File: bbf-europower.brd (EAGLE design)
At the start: 16.5 x 52.1 mm, 9 parts

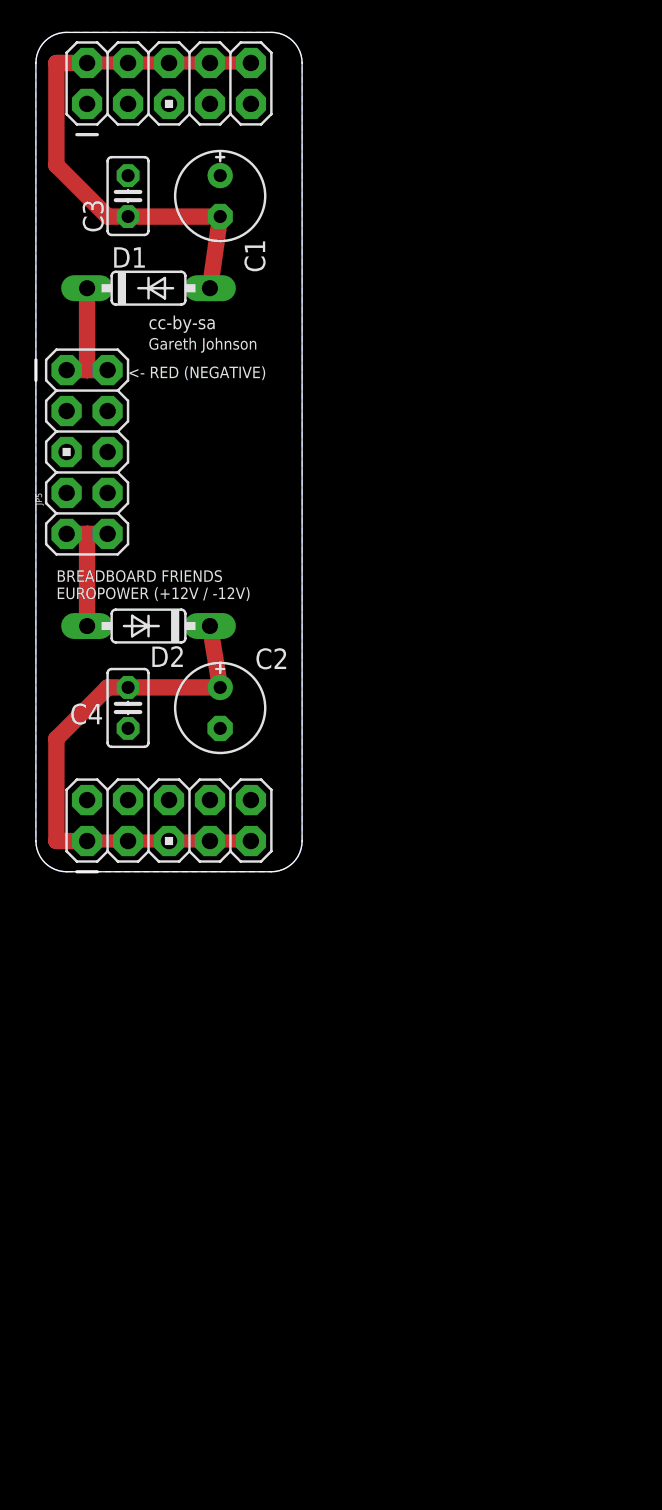
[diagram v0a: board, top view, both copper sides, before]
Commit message: Add files via upload
Through-hole versions of Thomas Hopman's revision of the bbf-europower.
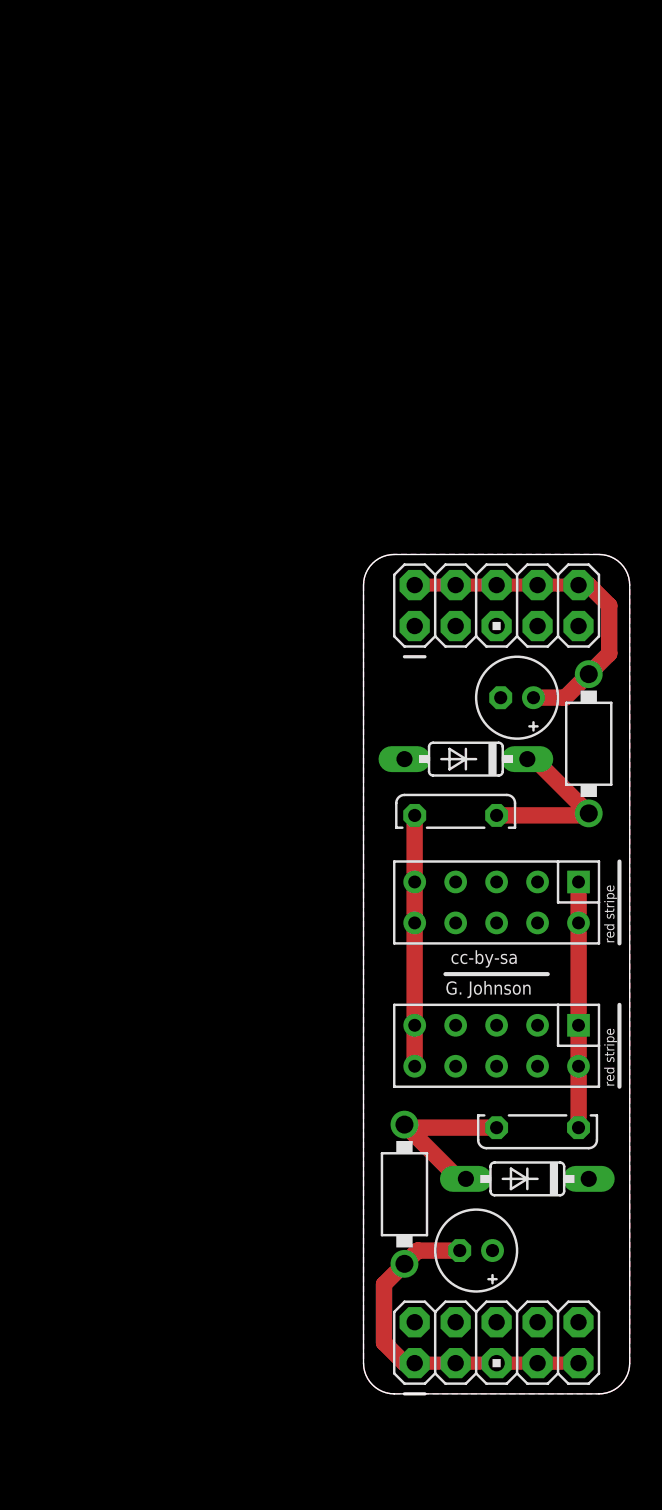
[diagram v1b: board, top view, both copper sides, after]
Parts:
- removed C3, C4: (no value), TomW:C025-025X050
- removed JP5: M05X2PTH, SparkFun:AVR_ICSP
- added +FUSE1: +FUSE, TomW:C050H075X075
- added -FUSE1: -FUSE, TomW:C050H075X075
- added J1, J2: CON_HEADER_2X05-PTH, tomatek:M2X5
- added L1, L2: (no value), GazJ:FBS
- C1, C2: value (none) -> 47u; device resistor:E2,5-6E -> resistor:E2-5
- D1, D2: value 1N4148DO35-7 -> 1N5819HW
- moved D2 41.6 mm to (10.2, 13.3)
- moved JP2 38.2 mm to (8.26, 3.17)
- moved JP1 38.2 mm to (8.26, 48.9)
- moved C2 37.2 mm to (6.99, 8.89), turned to 180 degrees
- moved C1 36.2 mm to (9.53, 43.2), turned to 180 degrees
- moved D1 35.2 mm to (6.35, 39.4), turned to 180 degrees
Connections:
- removed net +VE: D2.A, JP5.10, JP5.9
- removed net -VE: D1.C, JP5.1, JP5.2
- removed net N$10: JP5.4, JP5.8
- removed net N$5: JP5.3, JP5.7
- new net +12V: +FUSE1.1, J1.10, J1.9, J2.10, J2.9
- new net -12V: -FUSE1.1, J1.1, J1.2, J2.1, J2.2
- new net N$38: +FUSE1.2, D1.C, L1.1
- new net N$39: -FUSE1.2, D2.A, L2.1
- net GND: now also C1.-, C2.+, D1.A, D2.C, J1.3, J1.4, J1.5, J1.6, J1.7, J1.8, J2.3, J2.4, J2.5, J2.6, J2.7, J2.8; no longer C1.+, C2.-, C3.2, C4.1, JP5.5, JP5.6
- net VCC: now also C1.+, L1.2; no longer C1.-, C3.1, D1.A
- net VEE: now also C2.-, L2.2; no longer C2.+, C4.2, D2.C
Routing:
- net +12V: track 0.00 -> 15.6 mm
- net -12V: track 0.00 -> 15.2 mm
- net VCC: track 34.4 -> 21.4 mm
- net VEE: track 33.8 -> 21.8 mm
- net N$39: track 0.00 -> 11.0 mm
- net N$38: track 0.00 -> 11.0 mm
- net +VE: track 8.26 -> 0.00 mm
- net -VE: track 7.62 -> 0.00 mm
- added copper zone on layer 1, net GND
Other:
- board text added: "G. Johnson"
- board text added: "red stripe"
- board text removed: "<- RED (NEGATIVE)"
- board text removed: "BREADBOARD FRIENDS EUROPOWER (+12V / -12V)"
- board text removed: "Gareth Johnson"

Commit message: adding the new 1x5 connector to ground - first attempt
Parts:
- added JP3: (no value), SparkFun:1X05
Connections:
- net GND: now also JP3.1, JP3.2, JP3.3, JP3.4, JP3.5
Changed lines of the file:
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@@
 <?xml version="1.0" encoding="utf-8"?>
 <!DOCTYPE eagle SYSTEM "eagle.dtd">
-<eagle version="7.3.0">
+<eagle version="9.6.2">
 <drawing>
 <settings>
-<setting alwaysvectorfont="yes"/>
+<setting alwaysvectorfont="no"/>
+<setting keepoldvectorfont="yes"/>
 <setting verticaltext="up"/>
 </settings>
@@
 <param name="dpMaxLengthDifference" value="10mm"/>
 <param name="dpGapFactor" value="2.5"/>
-<param name="checkGrid" value="0"/>
 <param name="checkAngle" value="1"/>
 <param name="checkFont" value="1"/>
 <param name="checkRestrict" value="1"/>
+<param name="checkStop" value="0"/>
+<param name="checkValues" value="0"/>
+<param name="checkNames" value="1"/>
+<param name="checkWireStubs" value="1"/>
+<param name="checkPolygonWidth" value="0"/>
 <param name="useDiameter" value="13"/>
 <param name="maxErrors" value="50"/>
@@
 <element name="+FUSE1" library="TomW" package="C050H075X075" value="+FUSE" x="5.715" y="35.8775" smashed="yes"/>
 <element name="-FUSE1" library="TomW" package="C050H075X075" value="-FUSE" x="10.795" y="16.51" smashed="yes" rot="R180"/>
+<element name="JP3" library="SparkFun" package="1X05" value="" x="1.905" y="-3.81" smashed="yes">
+<attribute name="NAME" x="0.5588" y="-1.9812" size="1.27" layer="25" ratio="10"/>
+<attribute name="VALUE" x="0.635" y="-6.985" size="1.27" layer="27"/>
+</element>
 </elements>
 <signals>
@@
 <vertex x="1.905" y="0"/>
 </polygon>
+<contactref element="JP3" pad="1"/>
+<contactref element="JP3" pad="5"/>
+<contactref element="JP3" pad="2"/>
+<contactref element="JP3" pad="3"/>
+<contactref element="JP3" pad="4"/>
+<wire x1="10.795" y1="47.625" x2="13.335" y2="47.625" width="0" layer="19" extent="1-1"/>
+<wire x1="8.255" y1="47.625" x2="10.795" y2="47.625" width="0" layer="19" extent="1-1"/>
+<wire x1="5.715" y1="47.625" x2="8.255" y2="47.625" width="0" layer="19" extent="1-1"/>
+<wire x1="3.175" y1="47.625" x2="5.715" y2="47.625" width="0" layer="19" extent="1-1"/>
+<wire x1="8.509" y1="43.18" x2="8.255" y2="47.625" width="0" layer="19" extent="1-1"/>
+<wire x1="2.54" y1="39.37" x2="8.509" y2="43.18" width="0" layer="19" extent="1-1"/>
+<wire x1="5.715" y1="31.75" x2="2.54" y2="39.37" width="0" layer="19" extent="1-1"/>
+<wire x1="8.255" y1="31.75" x2="5.715" y2="31.75" width="0" layer="19" extent="1-1"/>
+<wire x1="10.795" y1="31.75" x2="8.255" y2="31.75" width="0" layer="19" extent="1-1"/>
+<wire x1="10.795" y1="29.21" x2="10.795" y2="31.75" width="0" layer="19" extent="1-1"/>
+<wire x1="8.255" y1="29.21" x2="8.255" y2="31.75" width="0" layer="19" extent="1-1"/>
+<wire x1="5.715" y1="29.21" x2="5.715" y2="31.75" width="0" layer="19" extent="1-1"/>
+<wire x1="10.795" y1="22.86" x2="10.795" y2="29.21" width="0" layer="19" extent="1-1"/>
+<wire x1="8.255" y1="22.86" x2="10.795" y2="22.86" width="0" layer="19" extent="1-1"/>
+<wire x1="10.795" y1="20.32" x2="10.795" y2="22.86" width="0" layer="19" extent="1-1"/>
+<wire x1="5.715" y1="22.86" x2="8.255" y2="22.86" width="0" layer="19" extent="1-1"/>
+<wire x1="8.255" y1="20.32" x2="8.255" y2="22.86" width="0" layer="19" extent="1-1"/>
+<wire x1="5.715" y1="20.32" x2="5.715" y2="22.86" width="0" layer="19" extent="1-1"/>
+<wire x1="13.97" y1="13.335" x2="10.795" y2="20.32" width="0" layer="19" extent="1-1"/>
+<wire x1="8.001" y1="8.89" x2="13.97" y2="13.335" width="0" layer="19" extent="1-1"/>
+<wire x1="8.255" y1="4.445" x2="8.001" y2="8.89" width="0" layer="19" extent="1-1"/>
+<wire x1="10.795" y1="4.445" x2="8.255" y2="4.445" width="0" layer="19" extent="1-1"/>
+<wire x1="13.335" y1="4.445" x2="10.795" y2="4.445" width="0" layer="19" extent="1-1"/>
+<wire x1="5.715" y1="4.445" x2="8.255" y2="4.445" width="0" layer="19" extent="1-1"/>
+<wire x1="3.175" y1="4.445" x2="5.715" y2="4.445" width="0" layer="19" extent="1-1"/>
+<wire x1="12.065" y1="-3.81" x2="10.795" y2="4.445" width="0" layer="19" extent="1-1"/>
+<wire x1="9.525" y1="-3.81" x2="12.065" y2="-3.81" width="0" layer="19" extent="1-1"/>
+<wire x1="6.985" y1="-3.81" x2="9.525" y2="-3.81" width="0" layer="19" extent="1-1"/>
+<wire x1="4.445" y1="-3.81" x2="6.985" y2="-3.81" width="0" layer="19" extent="1-1"/>
+<wire x1="1.905" y1="-3.81" x2="4.445" y2="-3.81" width="0" layer="19" extent="1-1"/>
 </signal>
 <signal name="VCC">
@@
 </signal>
 </signals>
+<mfgpreviewcolors>
+<mfgpreviewcolor name="soldermaskcolor" color="0xC8008000"/>
+<mfgpreviewcolor name="silkscreencolor" color="0xFFFEFEFE"/>
+<mfgpreviewcolor name="backgroundcolor" color="0xFF282828"/>
+<mfgpreviewcolor name="coppercolor" color="0xFFFFBF00"/>
+<mfgpreviewcolor name="substratecolor" color="0xFF786E46"/>
+</mfgpreviewcolors>
 </board>
 </drawing>

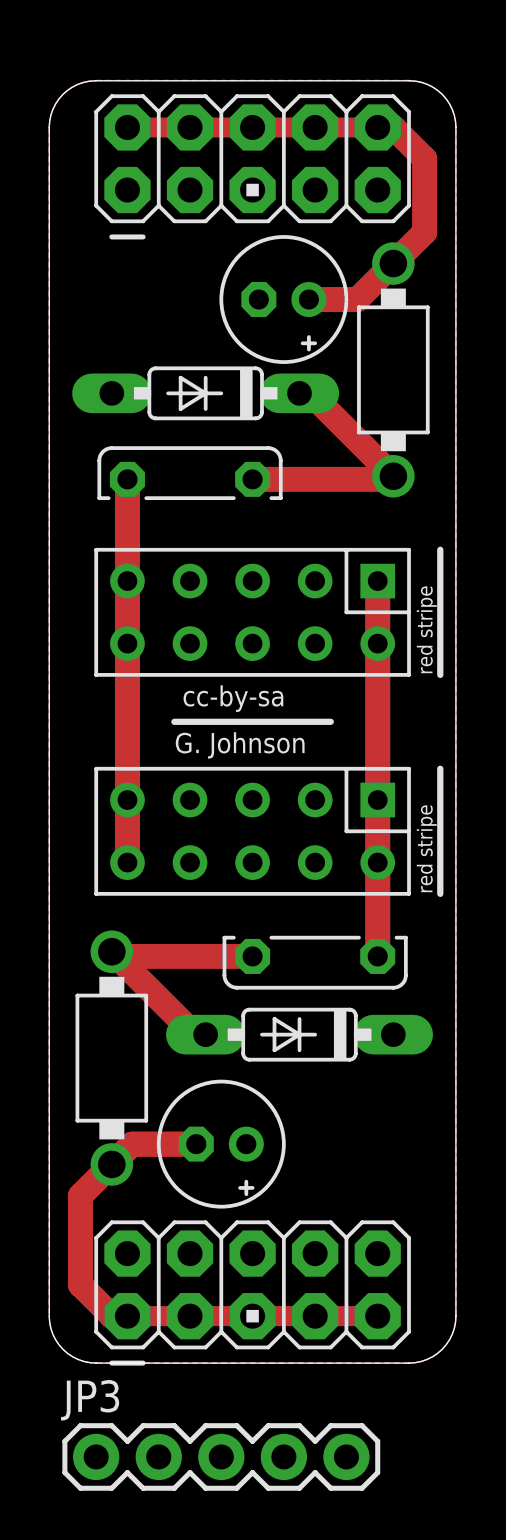
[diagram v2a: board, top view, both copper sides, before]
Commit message: the vcc with the farther away connector holes and wider board
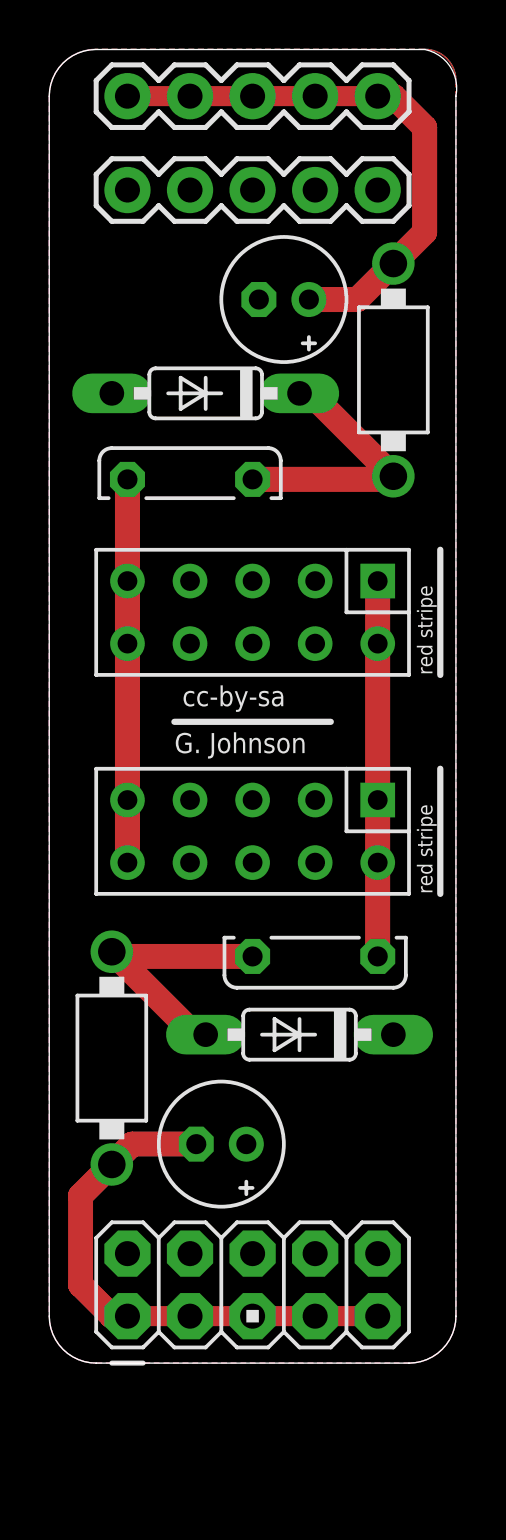
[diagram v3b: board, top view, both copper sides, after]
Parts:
- JP1: value M05X2PTH -> (none); device SparkFun:AVR_ICSP -> SparkFun:1X05
- moved JP3 51.5 mm to (3.17, 47.6)
- moved JP1 5.68 mm to (3.17, 51.4), turned to 0 degrees
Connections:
- net GND: no longer JP1.1, JP1.3, JP1.5, JP1.7, JP1.9
- net VCC: now also JP1.1, JP1.3, JP1.5; no longer JP1.10, JP1.6, JP1.8
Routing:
- net VCC: track 21.4 -> 22.7 mm
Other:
- board size 16.5 x 52.1 mm -> 16.5 x 53.3 mm
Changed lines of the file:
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@@
 <plain>
 <wire x1="14.605" y1="0" x2="16.51" y2="1.905" width="0" layer="20" curve="90"/>
-<wire x1="16.51" y1="1.905" x2="16.51" y2="50.165" width="0" layer="20"/>
-<wire x1="16.51" y1="50.165" x2="14.615" y2="52.06" width="0" layer="20" curve="90"/>
-<wire x1="14.615" y1="52.06" x2="1.895" y2="52.06" width="0" layer="20"/>
-<wire x1="1.895" y1="52.06" x2="0" y2="50.165" width="0" layer="20" curve="90"/>
-<wire x1="0" y1="50.165" x2="0" y2="1.905" width="0" layer="20"/>
+<wire x1="16.51" y1="1.905" x2="16.51" y2="51.435" width="0" layer="20"/>
+<wire x1="16.51" y1="51.435" x2="15.25" y2="53.33" width="0" layer="20" curve="90"/>
+<wire x1="15.25" y1="53.33" x2="1.895" y2="53.33" width="0" layer="20"/>
+<wire x1="1.895" y1="53.33" x2="0" y2="51.435" width="0" layer="20" curve="90"/>
+<wire x1="0" y1="51.435" x2="0" y2="1.905" width="0" layer="20"/>
 <wire x1="0" y1="1.905" x2="1.905" y2="0" width="0" layer="20" curve="90"/>
 <wire x1="1.905" y1="0" x2="14.605" y2="0" width="0" layer="20"/>
@@
 </autorouter>
 <elements>
-<element name="JP1" library="SparkFun" package="AVR_ICSP" value="M05X2PTH" x="8.255" y="48.895" smashed="yes" rot="R90"/>
 <element name="JP2" library="SparkFun" package="AVR_ICSP" value="M05X2PTH" x="8.255" y="3.175" smashed="yes" rot="R90"/>
 <element name="J1" library="tomatek" package="M2X5" value="CON_HEADER_2X05-PTH" x="8.255" y="30.48" smashed="yes" rot="R180"/>
@@
 <element name="+FUSE1" library="TomW" package="C050H075X075" value="+FUSE" x="5.715" y="35.8775" smashed="yes"/>
 <element name="-FUSE1" library="TomW" package="C050H075X075" value="-FUSE" x="10.795" y="16.51" smashed="yes" rot="R180"/>
-<element name="JP3" library="SparkFun" package="1X05" value="" x="1.905" y="-3.81" smashed="yes">
-<attribute name="NAME" x="0.5588" y="-1.9812" size="1.27" layer="25" ratio="10"/>
-<attribute name="VALUE" x="0.635" y="-6.985" size="1.27" layer="27"/>
+<element name="JP3" library="SparkFun" package="1X05" value="" x="3.175" y="47.625" smashed="yes">
+<attribute name="VALUE" x="1.905" y="44.45" size="1.27" layer="27"/>
+</element>
+<element name="JP1" library="SparkFun" package="1X05" value="" x="3.175" y="51.435" smashed="yes">
+<attribute name="VALUE" x="1.905" y="48.26" size="1.27" layer="27"/>
 </element>
 </elements>
 <signals>
 <signal name="GND">
-<contactref element="JP1" pad="7"/>
-<contactref element="JP1" pad="5"/>
-<contactref element="JP1" pad="3"/>
-<contactref element="JP1" pad="1"/>
 <contactref element="JP2" pad="8"/>
 <contactref element="JP2" pad="6"/>
 <contactref element="JP2" pad="4"/>
 <contactref element="JP2" pad="2"/>
-<contactref element="JP1" pad="9"/>
 <contactref element="JP2" pad="10"/>
 <polygon width="0.254" layer="16" isolate="0.3048">
 <vertex x="14.605" y="0" curve="90"/>
 <vertex x="16.51" y="1.905"/>
-<vertex x="16.51" y="50.165" curve="90"/>
-<vertex x="14.605" y="52.07"/>
-<vertex x="1.905" y="52.07" curve="90"/>
-<vertex x="0" y="50.165"/>
+<vertex x="16.51" y="52.07" curve="90"/>
+<vertex x="15.24" y="53.34"/>
+<vertex x="1.905" y="53.34" curve="90"/>
+<vertex x="0" y="51.435"/>
 <vertex x="0" y="1.905" curve="90"/>
 <vertex x="1.905" y="0"/>
@@
 <vertex x="14.605" y="0" curve="90"/>
 <vertex x="16.51" y="1.905"/>
-<vertex x="16.51" y="50.165" curve="90"/>
-<vertex x="14.605" y="52.07"/>
-<vertex x="1.905" y="52.07" curve="90"/>
-<vertex x="0" y="50.165"/>
+<vertex x="16.51" y="52.07" curve="90"/>
+<vertex x="15.24" y="53.34"/>
+<vertex x="1.905" y="53.34" curve="90"/>
+<vertex x="0" y="51.435"/>
 <vertex x="0" y="1.905" curve="90"/>
 <vertex x="1.905" y="0"/>
@@
 <contactref element="JP3" pad="3"/>
 <contactref element="JP3" pad="4"/>
-<wire x1="10.795" y1="47.625" x2="13.335" y2="47.625" width="0" layer="19" extent="1-1"/>
-<wire x1="8.255" y1="47.625" x2="10.795" y2="47.625" width="0" layer="19" extent="1-1"/>
-<wire x1="5.715" y1="47.625" x2="8.255" y2="47.625" width="0" layer="19" extent="1-1"/>
-<wire x1="3.175" y1="47.625" x2="5.715" y2="47.625" width="0" layer="19" extent="1-1"/>
-<wire x1="8.509" y1="43.18" x2="8.255" y2="47.625" width="0" layer="19" extent="1-1"/>
 <wire x1="2.54" y1="39.37" x2="8.509" y2="43.18" width="0" layer="19" extent="1-1"/>
 <wire x1="5.715" y1="31.75" x2="2.54" y2="39.37" width="0" layer="19" extent="1-1"/>
@@
 <wire x1="5.715" y1="4.445" x2="8.255" y2="4.445" width="0" layer="19" extent="1-1"/>
 <wire x1="3.175" y1="4.445" x2="5.715" y2="4.445" width="0" layer="19" extent="1-1"/>
-<wire x1="12.065" y1="-3.81" x2="10.795" y2="4.445" width="0" layer="19" extent="1-1"/>
-<wire x1="9.525" y1="-3.81" x2="12.065" y2="-3.81" width="0" layer="19" extent="1-1"/>
-<wire x1="6.985" y1="-3.81" x2="9.525" y2="-3.81" width="0" layer="19" extent="1-1"/>
-<wire x1="4.445" y1="-3.81" x2="6.985" y2="-3.81" width="0" layer="19" extent="1-1"/>
-<wire x1="1.905" y1="-3.81" x2="4.445" y2="-3.81" width="0" layer="19" extent="1-1"/>
+<wire x1="13.335" y1="47.625" x2="10.795" y2="4.445" width="0" layer="19" extent="1-1"/>
+<wire x1="10.795" y1="47.625" x2="13.335" y2="47.625" width="0" layer="19" extent="1-1"/>
+<wire x1="8.255" y1="47.625" x2="10.795" y2="47.625" width="0" layer="19" extent="1-1"/>
+<wire x1="5.715" y1="47.625" x2="8.255" y2="47.625" width="0" layer="19" extent="1-1"/>
+<wire x1="3.175" y1="47.625" x2="5.715" y2="47.625" width="0" layer="19" extent="1-1"/>
 </signal>
 <signal name="VCC">
-<contactref element="JP1" pad="8"/>
-<contactref element="JP1" pad="6"/>
-<contactref element="JP1" pad="4"/>
-<contactref element="JP1" pad="2"/>
-<contactref element="JP1" pad="10"/>
-<wire x1="5.715" y1="50.165" x2="3.175" y2="50.165" width="0.8128" layer="1"/>
-<wire x1="8.255" y1="50.165" x2="5.715" y2="50.165" width="0.8128" layer="1"/>
-<wire x1="8.255" y1="50.165" x2="10.795" y2="50.165" width="0.8128" layer="1"/>
-<wire x1="10.795" y1="50.165" x2="13.335" y2="50.165" width="0.8128" layer="1"/>
 <contactref element="C1" pad="+"/>
 <contactref element="L1" pad="2"/>
 <wire x1="13.97" y1="44.6405" x2="15.24" y2="45.9105" width="1.016" layer="1"/>
-<wire x1="15.24" y1="45.9105" x2="15.24" y2="48.895" width="1.016" layer="1"/>
-<wire x1="15.24" y1="48.895" x2="13.97" y2="50.165" width="1.016" layer="1"/>
-<wire x1="13.97" y1="50.165" x2="13.335" y2="50.165" width="1.016" layer="1"/>
+<wire x1="15.24" y1="45.9105" x2="15.24" y2="50.165" width="1.016" layer="1"/>
+<wire x1="13.97" y1="51.435" x2="15.24" y2="50.165" width="1.016" layer="1"/>
 <wire x1="13.97" y1="44.6405" x2="12.5095" y2="43.18" width="1.016" layer="1"/>
 <wire x1="12.5095" y1="43.18" x2="10.541" y2="43.18" width="1.016" layer="1"/>
+<contactref element="JP1" pad="5"/>
+<contactref element="JP1" pad="1"/>
+<contactref element="JP1" pad="4"/>
+<contactref element="JP1" pad="3"/>
+<contactref element="JP1" pad="2"/>
+<wire x1="13.335" y1="51.435" x2="13.97" y2="51.435" width="1.016" layer="1"/>
+<wire x1="13.335" y1="51.435" x2="10.795" y2="51.435" width="0.8128" layer="1"/>
+<wire x1="10.795" y1="51.435" x2="8.255" y2="51.435" width="0.8128" layer="1"/>
+<wire x1="8.255" y1="51.435" x2="5.715" y2="51.435" width="0.8128" layer="1"/>
+<wire x1="5.715" y1="51.435" x2="3.175" y2="51.435" width="0.8128" layer="1"/>
 </signal>
 <signal name="VEE">
